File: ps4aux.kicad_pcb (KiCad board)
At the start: 2 copper layers, 15 x 25 mm, 2 parts, among them J1 USB3_A_PLUG, J2 PS4_AUX_RECP

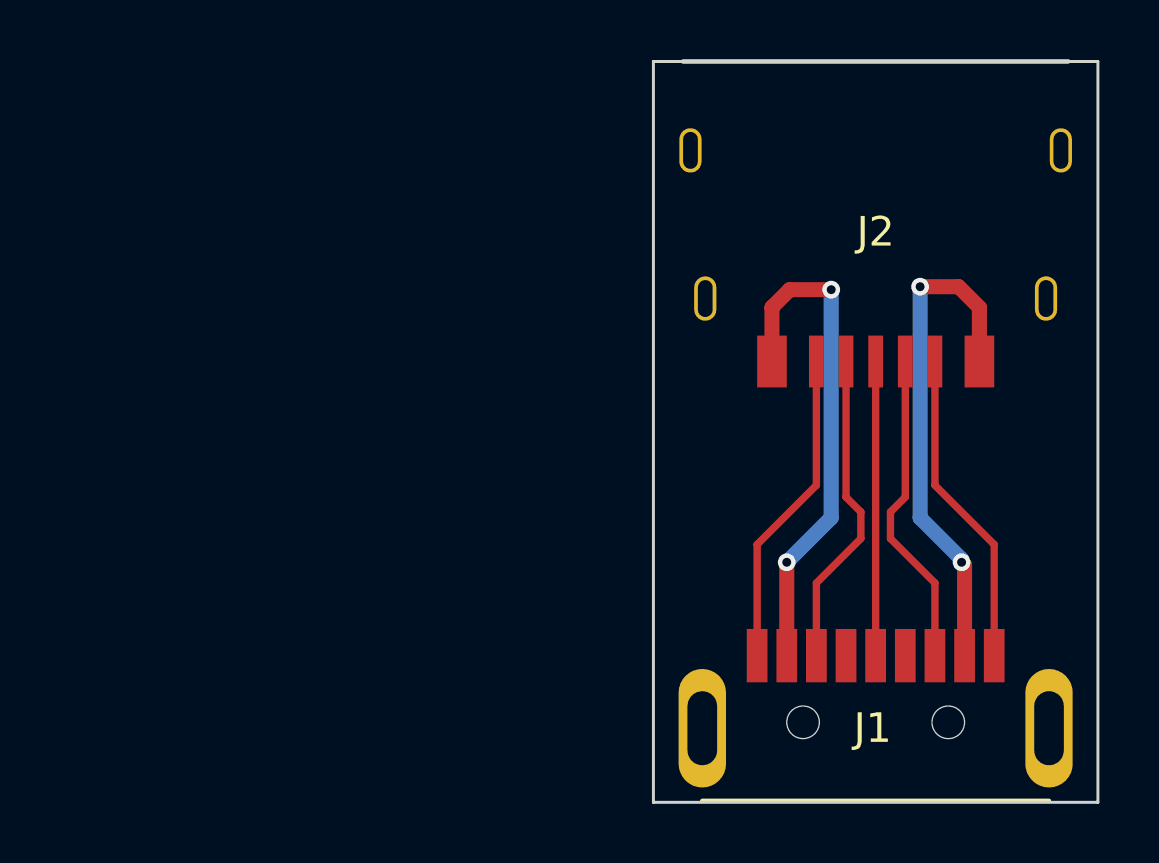
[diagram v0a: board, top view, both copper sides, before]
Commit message: Ground fill + shields for PS4AUX
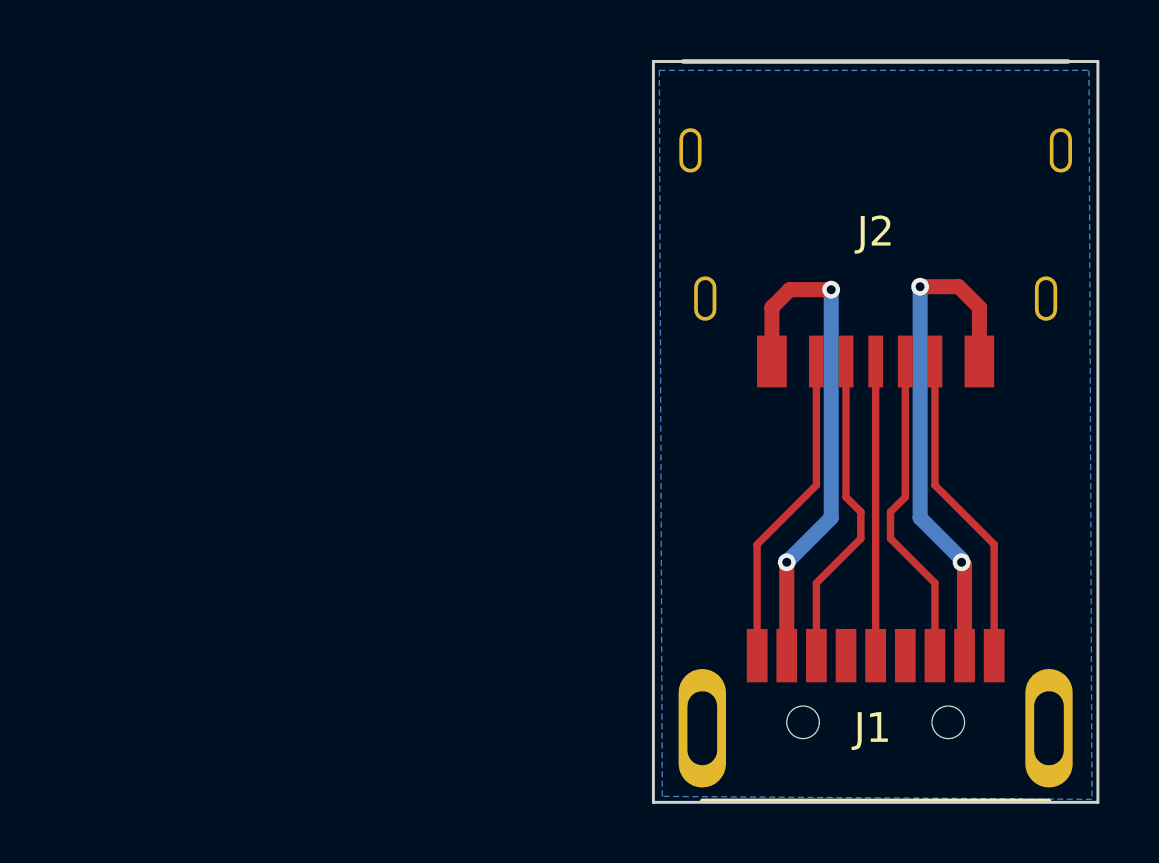
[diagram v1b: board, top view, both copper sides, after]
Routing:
- added copper zone on B.Cu, net GND
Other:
- rule via_min_size: 0.4 -> 0.3302
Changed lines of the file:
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@@
   (general
     (links 13)
-    (no_connects 6)
+    (no_connects 0)
     (area 0 0 0 0)
     (thickness 1.6)
@@
     (via_size 0.6)
     (via_drill 0.4)
-    (via_min_size 0.4)
+    (via_min_size 0.3302)
     (via_min_drill 0.3)
     (user_via 0.6858 0.3302)
@@
       (effects (font (size 1 1) (thickness 0.15)))
     )
-    (fp_text value USB3_A_PLUG (at -11.6011 4.8964) (layer F.Fab)
+    (fp_text value USB3_A_PLUG (at -11.6011 4.8964) (layer F.Fab) hide
       (effects (font (size 1 1) (thickness 0.15)))
     )
@@
       (effects (font (size 1 1) (thickness 0.15)))
     )
-    (fp_text value PS4_AUX_RECP (at 13.49 -4.61 180) (layer F.Fab)
+    (fp_text value PS4_AUX_RECP (at 13.49 -4.61 180) (layer F.Fab) hide
       (effects (font (size 1 1) (thickness 0.15)))
     )
@@
   (gr_line (start 115 100) (end 115 125) (angle 90) (layer Edge.Cuts) (width 0.1))
   (gr_line (start 100 100) (end 115 100) (angle 90) (layer Edge.Cuts) (width 0.1))
-  (segment (start 111 110.125) (end 111 108.3) (width 0.508) (layer F.Cu) (net 1) (status 400000))
-  (segment (start 110.5 117) (end 110.5 120.05) (width 0.508) (layer F.Cu) (net 1) (status 800000))
+  (segment (start 111 110.125) (end 111 108.3) (width 0.508) (layer F.Cu) (net 1))
+  (segment (start 110.5 117) (end 110.5 120.05) (width 0.508) (layer F.Cu) (net 1))
   (segment (start 110.4 116.9) (end 110.5 117) (width 0.508) (layer F.Cu) (net 1))
   (via (at 110.4 116.9) (size 0.6) (layers F.Cu B.Cu) (net 1))
@@
   (segment (start 110.3 107.6) (end 109 107.6) (width 0.508) (layer F.Cu) (net 1))
   (segment (start 111 108.3) (end 110.3 107.6) (width 0.508) (layer F.Cu) (net 1))
-  (segment (start 104 110.125) (end 104 108.3) (width 0.508) (layer F.Cu) (net 4) (status 400000))
-  (segment (start 104.5 116.9) (end 104.5 120.05) (width 0.508) (layer F.Cu) (net 4) (status 800000))
+  (segment (start 104 110.125) (end 104 108.3) (width 0.508) (layer F.Cu) (net 4))
+  (segment (start 104.5 116.9) (end 104.5 120.05) (width 0.508) (layer F.Cu) (net 4))
   (via (at 104.5 116.9) (size 0.6) (layers F.Cu B.Cu) (net 4))
   (segment (start 106 115.4) (end 104.5 116.9) (width 0.508) (layer B.Cu) (net 4))
@@
   (segment (start 111.5 116.3) (end 111.5 120.05) (width 0.25) (layer F.Cu) (net 9))
   (segment (start 109.5 114.3) (end 111.5 116.3) (width 0.25) (layer F.Cu) (net 9))
+  (zone (net 4) (net_name GND) (layer B.Cu) (hatch edge 0.508)
+    (connect_pads (clearance 0.508))
+    (min_thickness 0.254)
+    (fill yes (arc_segments 16) (thermal_gap 0.508) (thermal_bridge_width 0.508))
+    (polygon
+      (pts
+        (xy 100.2 100.3) (xy 114.7 100.3) (xy 114.8 124.9) (xy 100.3 124.8)
+      )
+    )
+  )
 )

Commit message: re-do board with circular drills
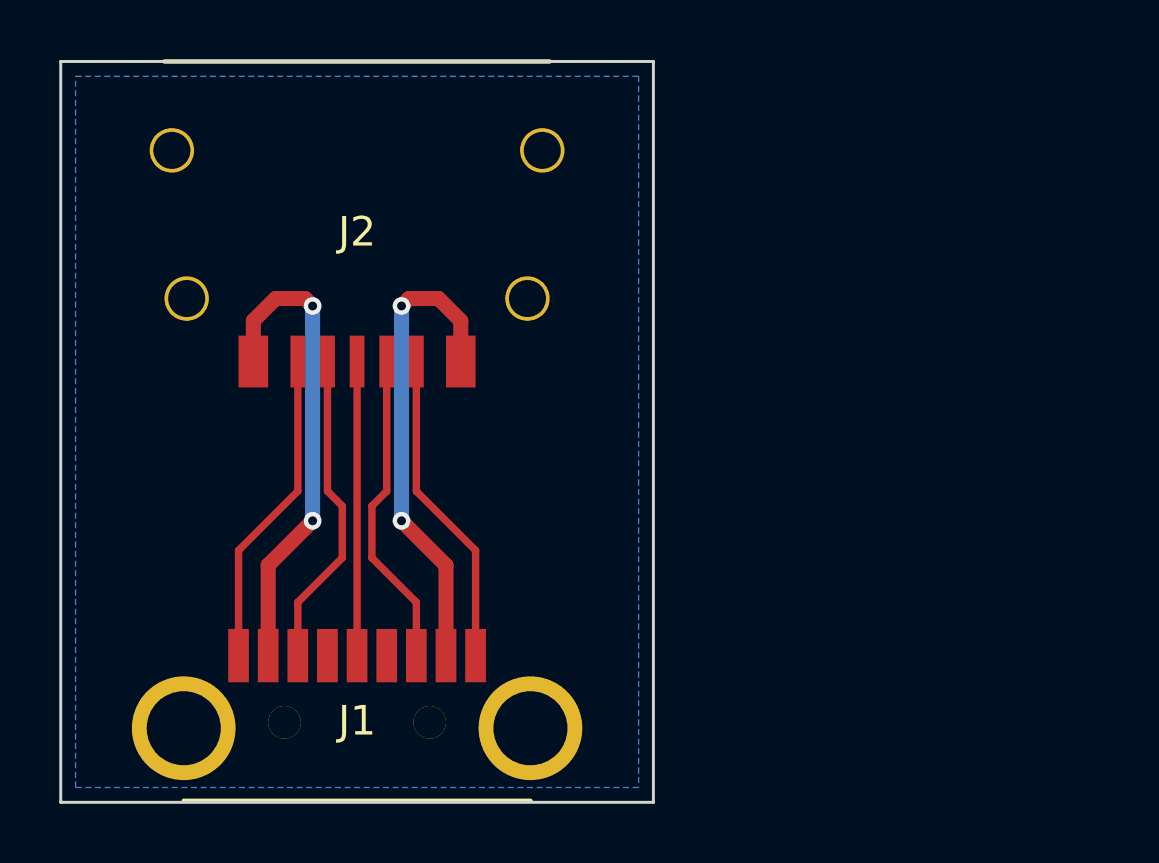
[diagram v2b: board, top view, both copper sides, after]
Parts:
- moved J1 17.5 mm to (90.0, 122.3)
- moved J2 17.5 mm to (90.0, 110.0)
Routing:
- net Net-(J1-Pad1): track 17.2 -> 16.2 mm
- net GND: track 17.0 -> 16.2 mm
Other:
- board size 15 x 25 mm -> 20 x 25 mm
- rule via_min_size: 0.3302 -> 0.4
